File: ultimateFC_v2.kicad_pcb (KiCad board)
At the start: 8 copper layers, 30.4 x 25.2 mm, 202 parts, among them J1 USB_B_Micro, J2 10132797-011100LF, J3 10132797-011100LF, J4 10132797-011100LF, J5 10132797-011100LF, J6 10132797-011100LF, Q1 DMP2066LSN-7, U1 EFM8BB21F16G-C-QFN20R, U10 NCP81253MNTBG, U11 SiZ200DT, U12 NCP81253MNTBG, U13 SiZ200DT, U14 TPS62821, U15 SiZ200DT, U16 NCP81253MNTBG, U17 NCP81253MNTBG, U18 NCP81253MNTBG, U19 NCP81253MNTBG, U2 EFM8BB21F16G-C-QFN20R, U20 SiZ200DT, U21 SiZ200DT, U22 SiZ200DT, U23 SiZ200DT, U24 EFM8BB21F16G-C-QFN20R, U25 NCP81253MNTBG, U26 SiZ200DT, U27 NCP81253MNTBG, U28 NCP81253MNTBG, U29 SiZ200DT, U3 NCP81253MNTBG, U30 SiZ200DT, U31 INA186, U32 LMR33630CQRNX, U33 STM32F745VGHx, U34 AB7456, U35 ZOE-M8Q_ZOE-M8Q, U36 ICM-20602, U37 S25FL064L, U39 BMP280, U4 SiZ200DT, U5 TPS630701, U6 EFM8BB21F16G-C-QFN20R, U7 NCP81253MNTBG, U8 SiZ200DT, U9 NCP81253MNTBG, X1 Molex_734120110, Y1 CSTNE8M00G550000R0, Y2 ECS-270-8-47Q-CES-TR

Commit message: update layout
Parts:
- removed the REF** at (197.1, 64.1) (x2)
- added REF**: Fiducial_0.5mm_Dia_1mm_Outer, Fiducial:Fiducial_0.5mm_Dia_1mm_Outer, F.Cu at (197.1, 64.1)
- added REF**: Fiducial_0.5mm_Dia_1mm_Outer, Fiducial:Fiducial_0.5mm_Dia_1mm_Outer, B.Cu at (197.1, 64.1)
- C1, C2: footprint Capacitor_SMD:C_1206_3216Metric -> Capacitor_SMD:C_0805_2012Metric
- moved FB2 3.95 mm to (178.4, 69.0), turned to 180 degrees
- moved C5 2.84 mm to (175.6, 67.6), turned to 180 degrees
- moved FB1 1.78 mm to (178.2, 74.8), turned to 270 degrees
- moved L1 1.42 mm to (179.1, 71.9)
- moved C4 0.99 mm to (175.6, 69.1)
- moved C3 0.98 mm to (174.3, 71.0)
- moved U5 0.93 mm to (176.2, 71.5)
- moved C2 0.66 mm to (175.4, 74.2)
- moved C1 0.46 mm to (175.4, 75.8)
- moved R37 0.16 mm to (180.6, 76.2)
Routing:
- net Net-(C1-Pad1): track 12.2 -> 1.48 mm
- net Net-(J1-Pad2): track 15.8 -> 14.1 mm
- net UART1_RX: track 7.87 -> 6.34 mm
- net I2C_SDA: track 43.0 -> 41.7 mm
- net Net-(J1-Pad3): track 15.0 -> 13.7 mm
- net USB_VBUS: track 25.8 -> 24.7 mm
- net MISO_FLASH: track 17.0 -> 16.0 mm
- net UART1_TX: track 7.93 -> 6.94 mm
- net Net-(C4-Pad1): track 5.29 -> 6.25 mm, vias 0 -> 2
- net Net-(L1-Pad2): track 2.95 -> 2.18 mm
- net Net-(J6-Pad10): track 20.2 -> 19.5 mm
- net MP_PIN5: track 22.2 -> 21.5 mm
- net Ap_ESC_2: track 7.01 -> 7.73 mm
- net +3V3: track 27.6 -> 28.4 mm
- net MP_PIN6: track 20.8 -> 20.2 mm
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- added copper zone on B.Cu, net Net-(C1-Pad1)
- added copper zone on B.Cu, net Net-(C4-Pad1)

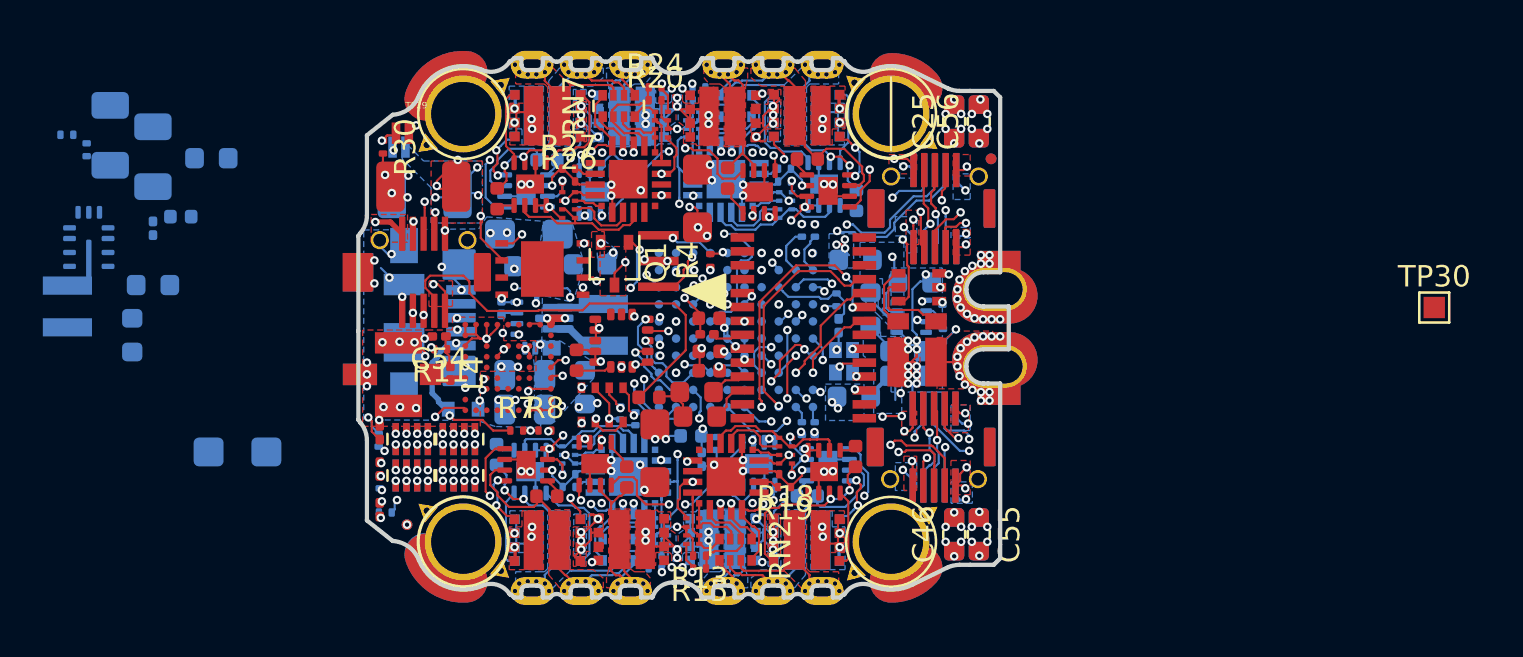
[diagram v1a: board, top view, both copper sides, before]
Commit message: remove references on silk screen
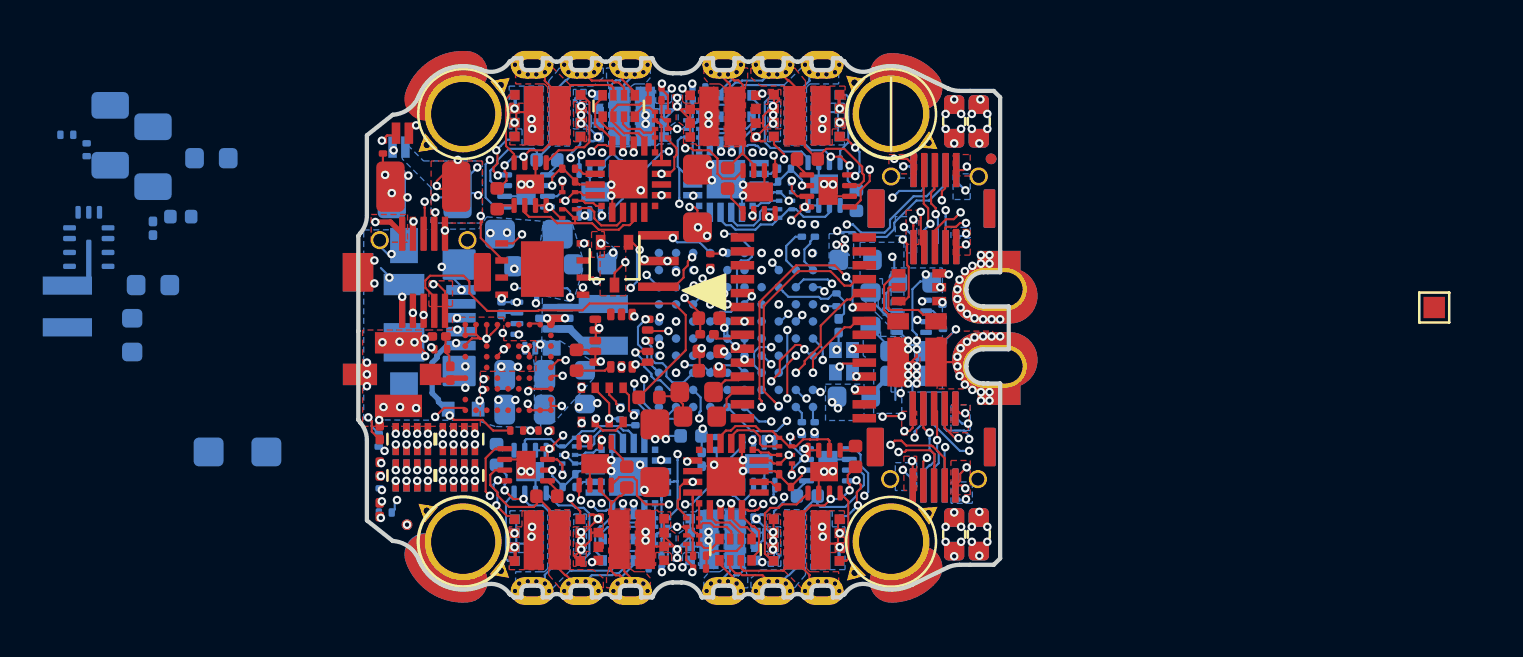
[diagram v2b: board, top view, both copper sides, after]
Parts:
- removed the REF** at (197.1, 64.1) (x2)
- added REF**: Fiducial_0.5mm_Dia_1mm_Outer, Fiducial:Fiducial_0.5mm_Dia_1mm_Outer, F.Cu at (197.1, 64.1)
- added REF**: Fiducial_0.5mm_Dia_1mm_Outer, Fiducial:Fiducial_0.5mm_Dia_1mm_Outer, B.Cu at (197.1, 64.1)
